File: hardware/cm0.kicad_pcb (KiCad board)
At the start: 4 copper layers, 85 x 56 mm, 252 parts, among them J1 USB_A_Stacked, J10 AudioJack_PJ-342, J2 USB_C_Receptacle_USB2.0_14P, J3 USB_C_Receptacle_USB2.0_14P, J4 USB_C_Receptacle_USB2.0_14P, J5 GPDI_A, J6 Micro_SD_Card_Det1, J7 RJ45_Hanrun_HR913550A_Horizon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, J8 Conn_01x03, J9 Conn_02x20_Odd_Even, Q1 BSN20, Q2 AO3415A, Q3 BSN20, Q4 BSN20, Q5 MMBT3904, U1 H3, U10 SY6280AAC, U11 SY6280AAC, U12 SY6280AAC, U13 TPD2EUSB30, U14 TPD2EUSB30, U15 TPD2EUSB30, U16 TPD2EUSB30, U17 HUSB237, U18 TPD2EUSB30, U19 UCL0524P, U2 H5TQ4G63EFR, U20 UCL0524P, U21 EMMC5.1_BGA153, U22 AP6212, U23 UCL0524P, U3 SY8088, U4 SY8088, U5 SY8088, U6 SY8089A, U7 SY8113, U8 SY8088, U9 SY6280AAC, Y1 32kHz, Y2 26MHz, Y3 24MHz

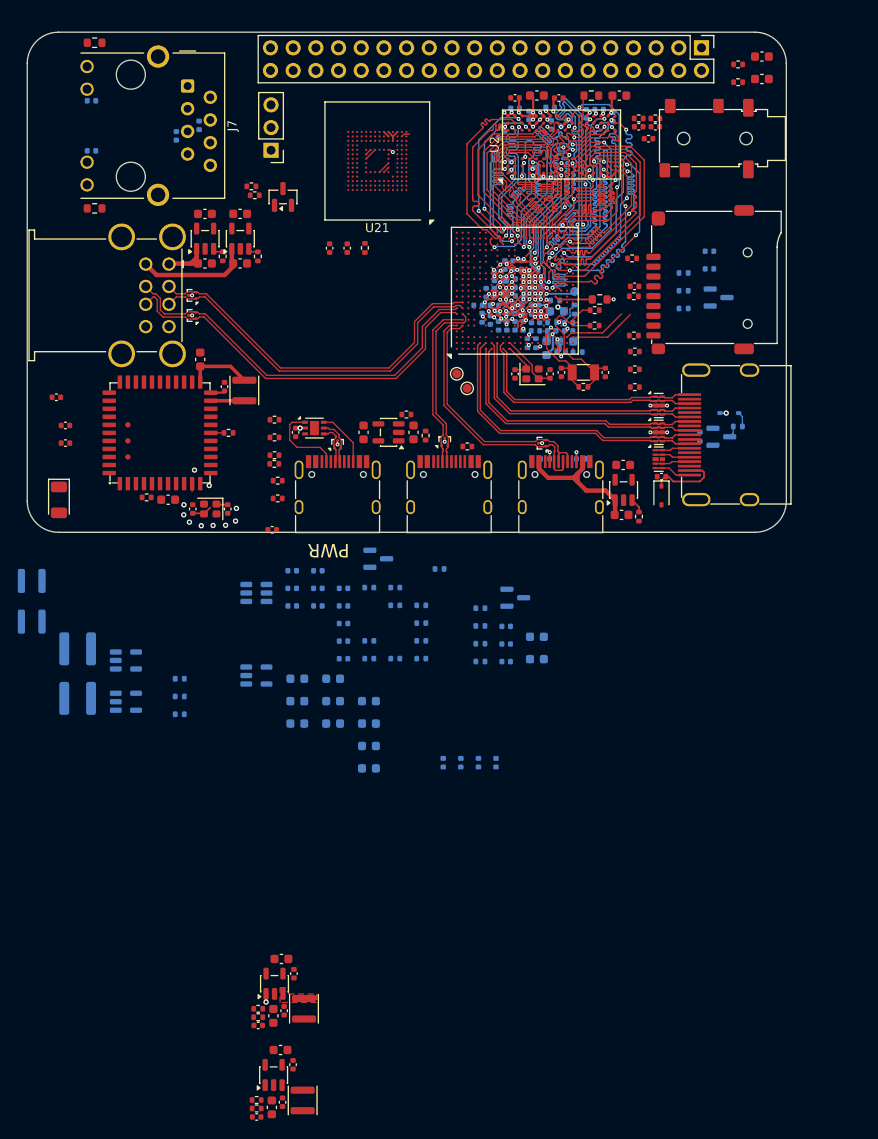
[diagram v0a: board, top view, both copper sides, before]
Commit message: Routed DCDC, EPHY and SD
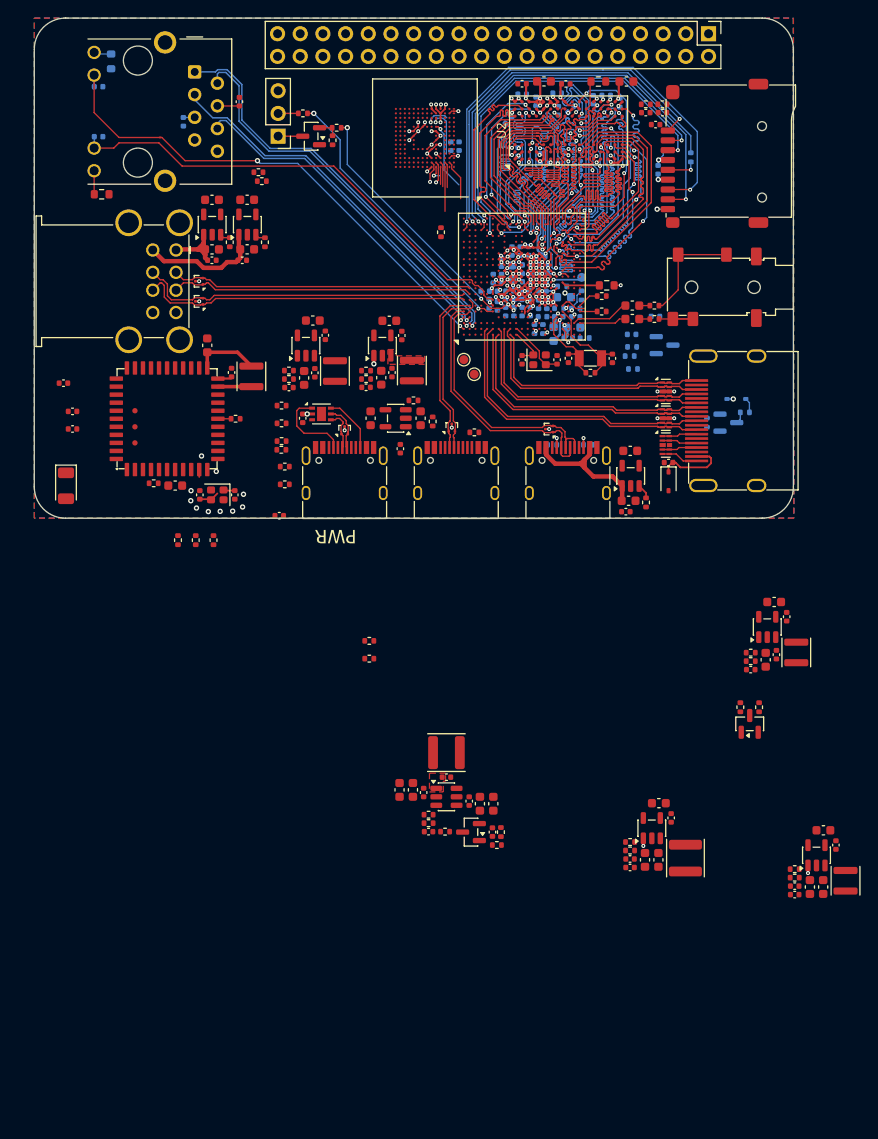
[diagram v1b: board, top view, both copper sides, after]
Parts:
- removed C74: 10uF, Capacitor_SMD:C_0603_1608Metric
- added C5: 22uF, Capacitor_SMD:C_0603_1608Metric, F.Cu at (150.2, 184.4)
- C101, C104, C121, C69, C70, C71, C72, C73, C75, C76, C77, C78, C79, C80, C81, C82, C83, C84, C85, C86, C87, C88, C89, C90, C91, C92, C93, C94, C95, C98, L3, L4, L5, L6, Q1, Q2, R10, R11, R15, R17, R18, R19, R20, R21, R22, R23, R24, R25, R26, R27, R28, R51, R69, R70, U5, U6, U7, U8: moved to F.Cu
- C109, C110, C111, R42, R43, R44, R55: moved to B.Cu
- moved L3 95.6 mm to (154.1, 183.8), turned to -90 degrees
- moved L6 86.0 mm to (148.6, 158.2), turned to -90 degrees
- moved C62 81.8 mm to (94.7, 126.9)
- moved C63 81.8 mm to (93.5, 127.4)
- moved R12 81.8 mm to (91.8, 127.6)
- moved R13 81.8 mm to (91.8, 126.6)
- moved U3 81.8 mm to (93.7, 123.8)
- moved C59 81.8 mm to (94.5, 121.0)
- moved C60 81.8 mm to (95.9, 122.7)
- moved L1 81.8 mm to (97.0, 126.7)
- moved C61 81.8 mm to (91.8, 128.5)
- moved U5 79.2 mm to (150.9, 180.9), turned to 90 degrees
- moved C65 72.5 mm to (104.5, 122.7)
- moved C66 72.5 mm to (100.5, 128.5)
- moved C67 72.5 mm to (103.4, 126.8)
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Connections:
- C109 pad 2: +3V3 -> +3V3_IO
- C72 pad 1: Net-(C72-Pad1) -> GND
- C73 pad 2: Net-(C72-Pad1) -> GND
- J6 pad 4: +3V3 -> +3V3_IO
- Q4 pad 1: +3V3 -> +3V3_IO
- R42 pad 1: +3V3 -> +3V3_IO
- R43 pad 1: +3V3 -> +3V3_IO
- R54 pad 1: +3V3 -> +3V3_IO
- R55 pad 1: +3V3 -> +3V3_IO
- R56 pad 1: +3V3 -> +3V3_IO
- U1 pad F10: /H3/TV_OUT -> /Audio/TV_OUT
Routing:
- net /H3/EPHY_LINK_LED: track 0.00 -> 57.3 mm, vias 0 -> 2
- net /H3/EPHY_SPD_LED: track 0.00 -> 53.9 mm
- net /H3/SD_D0: track 0.00 -> 53.8 mm, vias 0 -> 2
- net /H3/SD_D1: track 0.00 -> 51.0 mm, vias 0 -> 2
- net /H3/EPHY_TX+: track 0.00 -> 47.1 mm, vias 0 -> 1
- net /H3/EPHY_TX-: track 0.00 -> 45.2 mm, vias 0 -> 1
- net /H3/SD_CLK: track 0.00 -> 44.1 mm, vias 0 -> 1
- net /H3/SD_CMD: track 0.00 -> 42.9 mm, vias 0 -> 2
- net /H3/SD_D2: track 0.00 -> 42.6 mm, vias 0 -> 2
- net /H3/EPHY_RX+: track 0.00 -> 42.0 mm, vias 0 -> 1
- net /H3/SD_D3: track 0.00 -> 41.3 mm, vias 0 -> 2
- net /H3/EPHY_RX-: track 0.00 -> 38.2 mm, vias 0 -> 1
- net /GPIO/CPU_TX: track 0.00 -> 32.0 mm, vias 0 -> 2
- net /GPIO/CPU_RX: track 0.00 -> 29.2 mm, vias 0 -> 2
- net Net-(J10-Pad3): track 0.00 -> 12.2 mm
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- added copper zone on B.Cu, net GND
- added copper zone on F.Cu, net GND
- added copper zone on F.Cu, net Net-(U7-BS)
